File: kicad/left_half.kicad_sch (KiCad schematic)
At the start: 36 parts, among them SW1 SW_Push, SW10 SW_Push, SW11 SW_Push, SW12 SW_Push, SW13 SW_Push, SW14 SW_Push, SW15 SW_Push, SW16 SW_Push, SW17 SW_Push, SW18 SW_Push, SW2 SW_Push, SW3 SW_Push, SW4 SW_Push, SW5 SW_Push, SW6 SW_Push, SW7 SW_Push, SW8 SW_Push, SW9 SW_Push

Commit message: WiP: add schematic for the keyboard
- add full schematics for both halves
- add footprints and symbols for peripherals
- PIR still needs symbol + footprint
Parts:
- added J1: Conn_01x03_Pin, symbol Connector:Conn_01x03_Pin
- added J2: AudioJack4, symbol Connector_Audio:AudioJack4
- added R1: R_Photo, symbol Device:R_Photo
- added R2: R, symbol Device:R
- added U1: RP2040-Zero, symbol RP2040-Zero:RP2040-Zero
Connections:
- net C1: now reaches D1.1 (K), D10.1 (K), D11.1 (K), D12.1 (K), D13.1 (K), D14.1 (K), D15.1 (K), D16.1 (K), D17.1 (K), D18.1 (K), D2.1 (K), D3.1 (K), D4.1 (K), D5.1 (K), D6.1 (K), D7.1 (K), D8.1 (K), D9.1 (K), SW1.2, SW10.2, SW11.2, SW12.2, SW13.2, SW14.2, SW15.2, SW16.2, SW17.2, SW18.2, SW2.2, SW3.2, SW4.2, SW5.2, SW6.2, SW7.2, SW8.2, SW9.2
- net C1: now also U1.10, U1.11, U1.12, U1.13, U1.5, U1.6, U1.7, U1.8, U1.9
- new net ADC0: R1.2, R2.2, U1.26
- new net GND: J1.1 (Pin_1), J2.S, R2.1, U1.GND
- new net OUT: J1.2 (Pin_2), U1.28
- new net Rx: J2.R2, U1.1
- new net Tx: J2.R1, U1.0
- new net VCC: J1.3 (Pin_3), J2.T, R1.1, U1.3v3

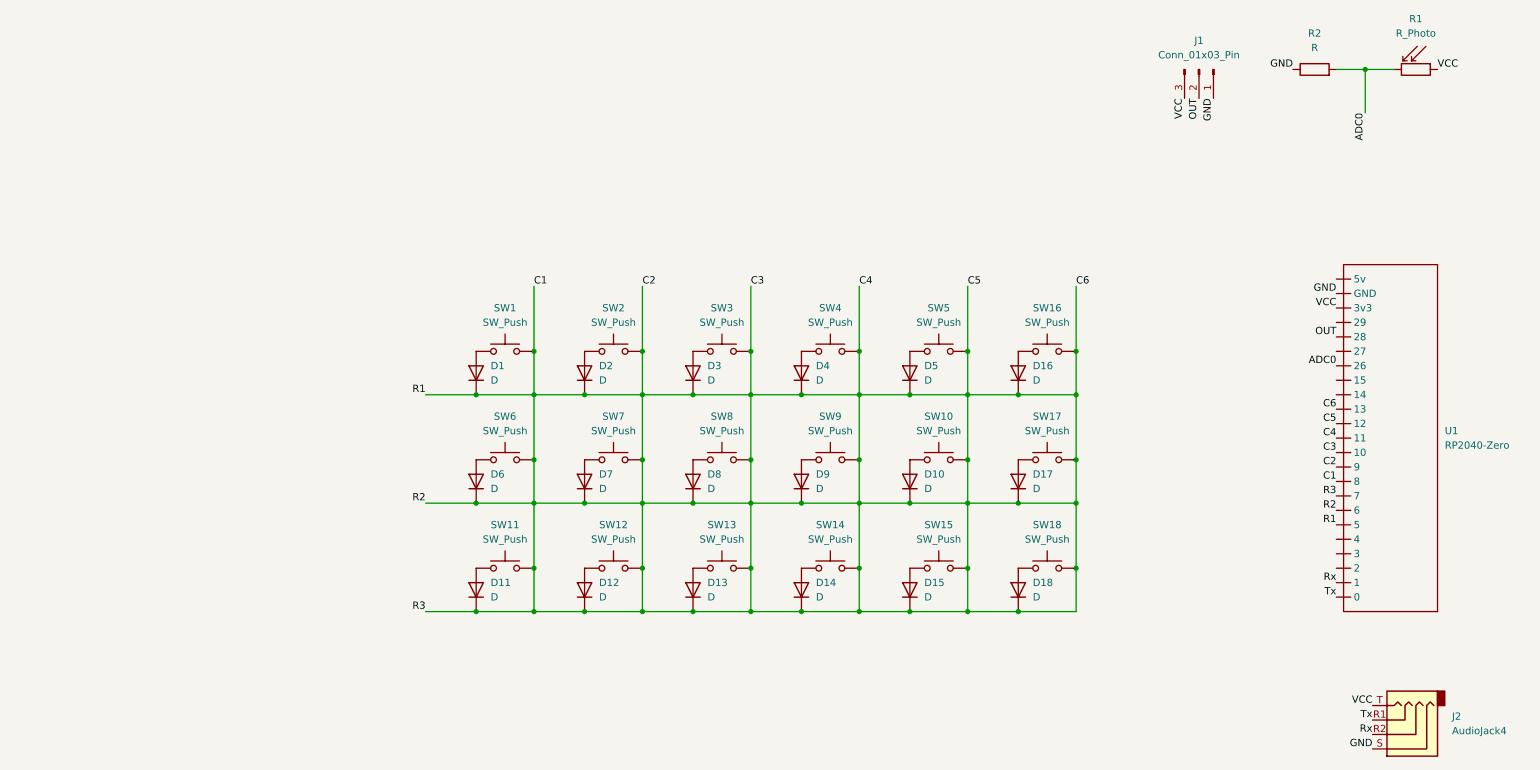
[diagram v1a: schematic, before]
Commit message: feat: add SK6812 per key lighting
- every key is illuminated by a SK6812 RGB LED
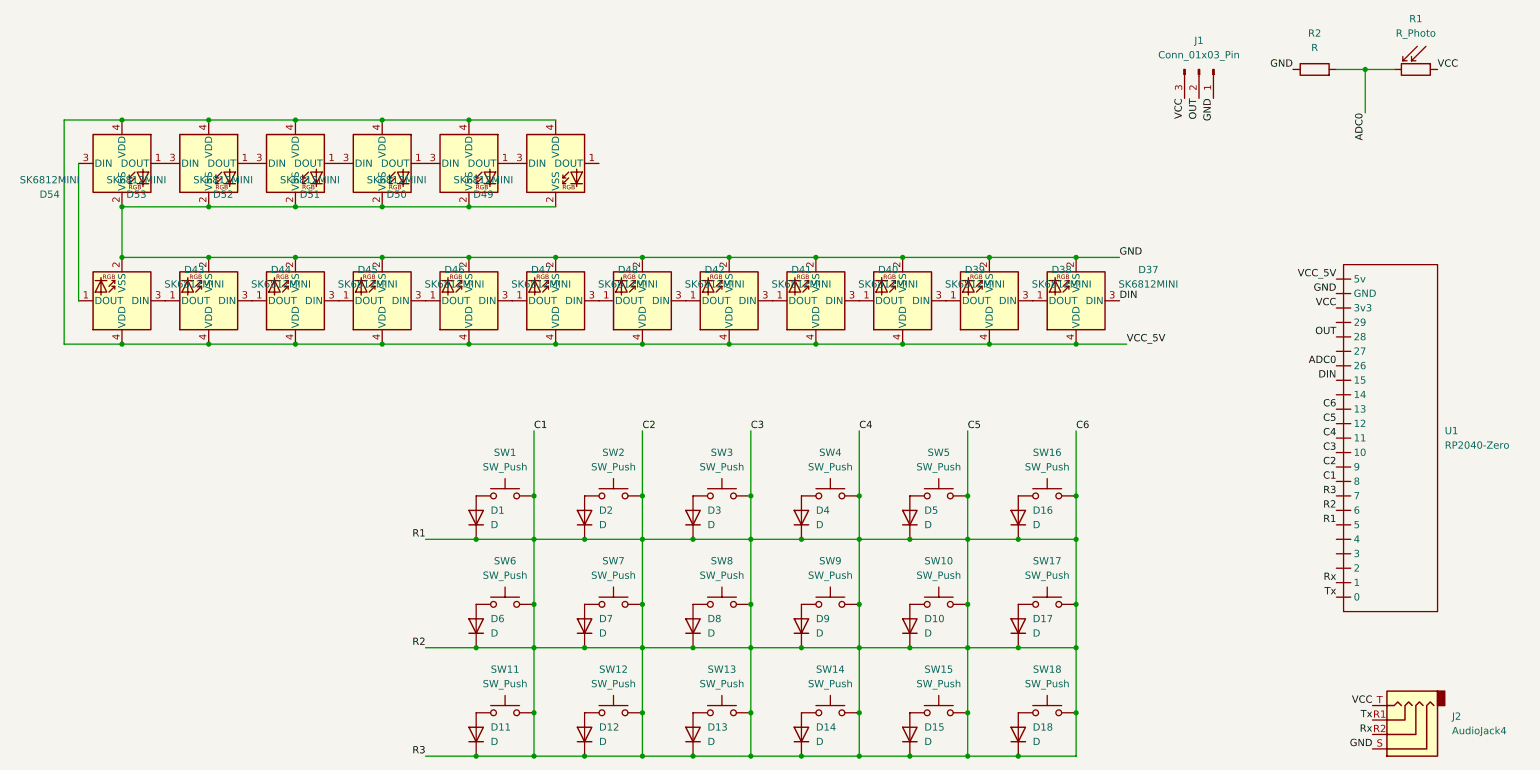
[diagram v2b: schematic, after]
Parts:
- added D37, D38, D39, D40, D41, D42, D43, D44, D45, D46, D47, D48, D49, D50, D51, D52, D53, D54: SK6812MINI, LED_SMD:LED_SK6812MINI_PLCC4_3.5x3.5mm_P1.75mm, symbol LED:SK6812MINI
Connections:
- net GND: now also D37.2 (VSS), D38.2 (VSS), D39.2 (VSS), D40.2 (VSS), D41.2 (VSS), D42.2 (VSS), D43.2 (VSS), D44.2 (VSS), D45.2 (VSS), D46.2 (VSS), D47.2 (VSS), D48.2 (VSS), D49.2 (VSS), D50.2 (VSS), D51.2 (VSS), D52.2 (VSS), D53.2 (VSS), D54.2 (VSS)
- net DIN: now reaches U1.15
- net DIN: now also D37.3 (DIN)
- net VCC_5V: now reaches U1.5v
- net VCC_5V: now also D37.4 (VDD), D38.4 (VDD), D39.4 (VDD), D40.4 (VDD), D41.4 (VDD), D42.4 (VDD), D43.4 (VDD), D44.4 (VDD), D45.4 (VDD), D46.4 (VDD), D47.4 (VDD), D48.4 (VDD), D49.4 (VDD), D50.4 (VDD), D51.4 (VDD), D52.4 (VDD), D53.4 (VDD), D54.4 (VDD)
- new net: D49.3 (DIN), D50.1 (DOUT)
- new net: D50.3 (DIN), D51.1 (DOUT)
- new net: D40.1 (DOUT), D41.3 (DIN)
- new net: D39.1 (DOUT), D40.3 (DIN)
- new net: D43.3 (DIN), D44.1 (DOUT)
- new net: D44.3 (DIN), D45.1 (DOUT)
- new net: D53.3 (DIN), D54.1 (DOUT)
- new net: D43.1 (DOUT), D54.3 (DIN)
- new net: D51.3 (DIN), D52.1 (DOUT)
- new net: D52.3 (DIN), D53.1 (DOUT)
- new net: D38.1 (DOUT), D39.3 (DIN)
- new net: D37.1 (DOUT), D38.3 (DIN)
- new net: D45.3 (DIN), D46.1 (DOUT)
- new net: D46.3 (DIN), D47.1 (DOUT)
- new net: D47.3 (DIN), D48.1 (DOUT)
- new net: D42.1 (DOUT), D48.3 (DIN)
- new net: D41.1 (DOUT), D42.3 (DIN)
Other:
- moved on the sheet: D1, D10, D11, D12, D13, D14, D15, D16, D17, D18, D2, D3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

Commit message: apply footprints for all components
- treat column 6 as individual thumbpad file that is connected via pogo
  pins
- use generic headers for components on external boards (like OLED)
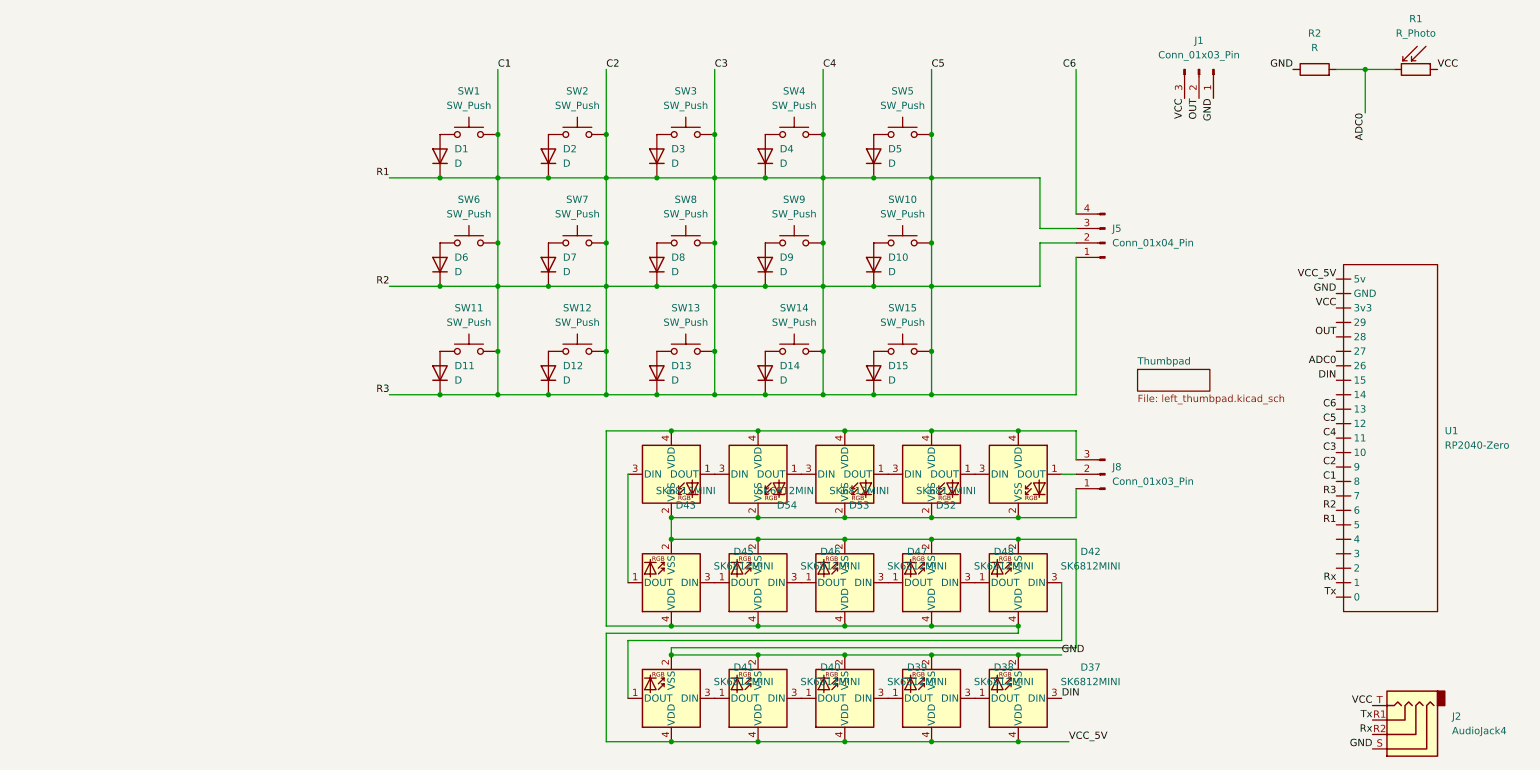
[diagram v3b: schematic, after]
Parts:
- removed D16, D17, D18: D, symbol Device:D
- removed D49, D50, D51: SK6812MINI, LED_SMD:LED_SK6812MINI_PLCC4_3.5x3.5mm_P1.75mm, symbol LED:SK6812MINI
- removed SW16, SW17, SW18: SW_Push, symbol Switch:SW_Push
- added J5: Conn_01x04_Pin, Connector_PinSocket_2.54mm:PinSocket_1x04_P2.54mm_Vertical, symbol Connector:Conn_01x04_Pin
- added J8: Conn_01x03_Pin, Connector_PinSocket_2.54mm:PinSocket_1x03_P2.54mm_Vertical, symbol Connector:Conn_01x03_Pin
- D1, D10, D11, D12, D13, D14, D15, D2, D3, D4, D5, D6, D7, D8, D9: footprint (none) -> Diode_THT:D_DO-35_SOD27_P7.62mm_Horizontal
- J1: footprint (none) -> Connector_PinHeader_2.54mm:PinHeader_1x03_P2.54mm_Vertical
- J2: footprint (none) -> PJ-320A:PJ-320A
- R1: footprint (none) -> OptoDevice:R_LDR_5.1x4.3mm_P3.4mm_Vertical
- R2: footprint (none) -> Resistor_THT:R_Axial_DIN0204_L3.6mm_D1.6mm_P7.62mm_Horizontal
- SW1, SW10, SW11, SW12, SW13, SW14, SW15, SW2, SW3, SW4, SW5, SW6, SW7, SW8, SW9: footprint (none) -> Choc-V1:Kailh-PG1353-Solderable-1U
- U1: footprint (none) -> RP2040-Zero:RP2040-Zero
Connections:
- net C1: now also J5.1 (Pin_1), J5.2 (Pin_2), J5.3 (Pin_3); no longer U1.13
- net GND: now also J8.1 (Pin_1)
- net VCC_5V: now also J8.3 (Pin_3)
- net at D52.1 (DOUT): now also J8.2 (Pin_2)
- new net C6: J5.4 (Pin_4), U1.13
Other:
- added sheet Thumbpad (left_thumbpad.kicad_sch)
- moved on the sheet: D1, D10, D11, D12, D13, D14, D15, D2, D3, D37, D38, D39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

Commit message: wip: add PCB
- started working on the actual PCB
- however this will be subject to change later
- add footprint for sk6812-mini-e LEDs
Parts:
- D37, D38, D39, D40, D41, D42, D43, D44, D45, D46, D47, D48, D52, D53, D54: footprint LED_SMD:LED_SK6812MINI_PLCC4_3.5x3.5mm_P1.75mm -> SK6812-Mini-E:MX_SK6812MINI-E
- SW1, SW10, SW11, SW12, SW13, SW14, SW15, SW2, SW3, SW4, SW5, SW6, SW7, SW8, SW9: footprint Choc-V1:Kailh-PG1353-Solderable-1U -> Choc-V1:SW_Kailh_Choc_V1
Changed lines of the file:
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@@
 			)
 		)
-		(property "Footprint" "LED_SMD:LED_SK6812MINI_PLCC4_3.5x3.5mm_P1.75mm"
+		(property "Footprint" "SK6812-Mini-E:MX_SK6812MINI-E"
 			(at 133.35 134.62 0)
 			(effects
@@
 			)
 		)
-		(property "Footprint" "Choc-V1:Kailh-PG1353-Solderable-1U"
+		(property "Footprint" "Choc-V1:SW_Kailh_Choc_V1"
 			(at 83.82 57.15 0)
 			(effects
@@
 			)
 		)
-		(property "Footprint" "Choc-V1:Kailh-PG1353-Solderable-1U"
+		(property "Footprint" "Choc-V1:SW_Kailh_Choc_V1"
 			(at 140.97 76.2 0)
 			(effects
@@
 			)
 		)
-		(property "Footprint" "Choc-V1:Kailh-PG1353-Solderable-1U"
+		(property "Footprint" "Choc-V1:SW_Kailh_Choc_V1"
 			(at 160.02 57.15 0)
 			(effects
@@
 			)
 		)
-		(property "Footprint" "LED_SMD:LED_SK6812MINI_PLCC4_3.5x3.5mm_P1.75mm"
+		(property "Footprint" "SK6812-Mini-E:MX_SK6812MINI-E"
 			(at 120.65 110.49 0)
 			(effects
@@
 			)
 		)
-		(property "Footprint" "Choc-V1:Kailh-PG1353-Solderable-1U"
+		(property "Footprint" "Choc-V1:SW_Kailh_Choc_V1"
 			(at 121.92 76.2 0)
 			(effects
@@
 			)
 		)
-		(property "Footprint" "LED_SMD:LED_SK6812MINI_PLCC4_3.5x3.5mm_P1.75mm"
+		(property "Footprint" "SK6812-Mini-E:MX_SK6812MINI-E"
 			(at 151.13 110.49 0)
 			(effects
@@
 			)
 		)
-		(property "Footprint" "Choc-V1:Kailh-PG1353-Solderable-1U"
+		(property "Footprint" "Choc-V1:SW_Kailh_Choc_V1"
 			(at 140.97 38.1 0)
 			(effects
@@
 			)
 		)
-		(property "Footprint" "Choc-V1:Kailh-PG1353-Solderable-1U"
+		(property "Footprint" "Choc-V1:SW_Kailh_Choc_V1"
 			(at 83.82 38.1 0)
 			(effects
@@
 			)
 		)
-		(property "Footprint" "LED_SMD:LED_SK6812MINI_PLCC4_3.5x3.5mm_P1.75mm"
+		(property "Footprint" "SK6812-Mini-E:MX_SK6812MINI-E"
 			(at 181.61 110.49 0)
 			(effects
@@
 			)
 		)
-		(property "Footprint" "LED_SMD:LED_SK6812MINI_PLCC4_3.5x3.5mm_P1.75mm"
+		(property "Footprint" "SK6812-Mini-E:MX_SK6812MINI-E"
 			(at 148.59 134.62 0)
 			(effects
@@
 			)
 		)
-		(property "Footprint" "LED_SMD:LED_SK6812MINI_PLCC4_3.5x3.5mm_P1.75mm"
+		(property "Footprint" "SK6812-Mini-E:MX_SK6812MINI-E"
 			(at 135.89 110.49 0)
 			(effects
@@
 			)
 		)
-		(property "Footprint" "Choc-V1:Kailh-PG1353-Solderable-1U"
+		(property "Footprint" "Choc-V1:SW_Kailh_Choc_V1"
 			(at 160.02 38.1 0)
 			(effects
@@
 			)
 		)
-		(property "Footprint" "Choc-V1:Kailh-PG1353-Solderable-1U"
+		(property "Footprint" "Choc-V1:SW_Kailh_Choc_V1"
 			(at 121.92 38.1 0)
 			(effects
@@
 			)
 		)
-		(property "Footprint" "LED_SMD:LED_SK6812MINI_PLCC4_3.5x3.5mm_P1.75mm"
+		(property "Footprint" "SK6812-Mini-E:MX_SK6812MINI-E"
 			(at 179.07 134.62 0)
 			(effects
@@
 			)
 		)
-		(property "Footprint" "LED_SMD:LED_SK6812MINI_PLCC4_3.5x3.5mm_P1.75mm"
+		(property "Footprint" "SK6812-Mini-E:MX_SK6812MINI-E"
 			(at 118.11 114.3 0)
 			(effects
@@
 			)
 		)
-		(property "Footprint" "LED_SMD:LED_SK6812MINI_PLCC4_3.5x3.5mm_P1.75mm"
+		(property "Footprint" "SK6812-Mini-E:MX_SK6812MINI-E"
 			(at 133.35 114.3 0)
 			(effects
@@
 			)
 		)
-		(property "Footprint" "LED_SMD:LED_SK6812MINI_PLCC4_3.5x3.5mm_P1.75mm"
+		(property "Footprint" "SK6812-Mini-E:MX_SK6812MINI-E"
 			(at 163.83 134.62 0)
 			(effects
@@
 			)
 		)
-		(property "Footprint" "LED_SMD:LED_SK6812MINI_PLCC4_3.5x3.5mm_P1.75mm"
+		(property "Footprint" "SK6812-Mini-E:MX_SK6812MINI-E"
 			(at 163.83 114.3 0)
 			(effects
@@
 			)
 		)
-		(property "Footprint" "LED_SMD:LED_SK6812MINI_PLCC4_3.5x3.5mm_P1.75mm"
+		(property "Footprint" "SK6812-Mini-E:MX_SK6812MINI-E"
 			(at 118.11 134.62 0)
 			(effects
@@
 			)
 		)
-		(property "Footprint" "LED_SMD:LED_SK6812MINI_PLCC4_3.5x3.5mm_P1.75mm"
+		(property "Footprint" "SK6812-Mini-E:MX_SK6812MINI-E"
 			(at 166.37 110.49 0)
 			(effects
@@
 			)
 		)
-		(property "Footprint" "Choc-V1:Kailh-PG1353-Solderable-1U"
+		(property "Footprint" "Choc-V1:SW_Kailh_Choc_V1"
 			(at 102.87 76.2 0)
 			(effects
@@
 			)
 		)
-		(property "Footprint" "Choc-V1:Kailh-PG1353-Solderable-1U"
+		(property "Footprint" "Choc-V1:SW_Kailh_Choc_V1"
 			(at 121.92 57.15 0)
 			(effects
@@
 			)
 		)
-		(property "Footprint" "Choc-V1:Kailh-PG1353-Solderable-1U"
+		(property "Footprint" "Choc-V1:SW_Kailh_Choc_V1"
 			(at 102.87 38.1 0)
 			(effects
@@
 			)
 		)
-		(property "Footprint" "Choc-V1:Kailh-PG1353-Solderable-1U"
+		(property "Footprint" "Choc-V1:SW_Kailh_Choc_V1"
 			(at 102.87 57.15 0)
 			(effects
@@
 			)
 		)
-		(property "Footprint" "Choc-V1:Kailh-PG1353-Solderable-1U"
+		(property "Footprint" "Choc-V1:SW_Kailh_Choc_V1"
 			(at 160.02 76.2 0)
 			(effects
@@
 			)
 		)
-		(property "Footprint" "Choc-V1:Kailh-PG1353-Solderable-1U"
+		(property "Footprint" "Choc-V1:SW_Kailh_Choc_V1"
 			(at 140.97 57.15 0)
 			(effects
@@
 			)
 		)
-		(property "Footprint" "Choc-V1:Kailh-PG1353-Solderable-1U"
+		(property "Footprint" "Choc-V1:SW_Kailh_Choc_V1"
 			(at 83.82 76.2 0)
 			(effects
@@
 			)
 		)
-		(property "Footprint" "LED_SMD:LED_SK6812MINI_PLCC4_3.5x3.5mm_P1.75mm"
+		(property "Footprint" "SK6812-Mini-E:MX_SK6812MINI-E"
 			(at 148.59 114.3 0)
 			(effects
@@
 			)
 		)
-		(property "Footprint" "LED_SMD:LED_SK6812MINI_PLCC4_3.5x3.5mm_P1.75mm"
+		(property "Footprint" "SK6812-Mini-E:MX_SK6812MINI-E"
 			(at 179.07 114.3 0)
 			(effects

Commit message: wip: pcb for both halves
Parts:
- removed J2: AudioJack4, PJ-320A:PJ-320A, symbol Connector_Audio:AudioJack4
- added J2: AudioJack4, PJ-320A:PJ-320A, symbol PJ-320A:AudioJack4
- SW1, SW10, SW11, SW12, SW13, SW14, SW15, SW2, SW3, SW4, SW5, SW6, SW7, SW8, SW9: footprint Choc-V1:SW_Kailh_Choc_V1 -> Choc-V1:SW_Kailh_Choc_V1_THT
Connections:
- net C1: no longer D1.1 (K), D10.1 (K), D11.1 (K), D12.1 (K), D13.1 (K), D14.1 (K), D15.1 (K), D2.1 (K), D3.1 (K), D4.1 (K), D5.1 (K), D6.1 (K), D7.1 (K), D8.1 (K), D9.1 (K), J5.1 (Pin_1), J5.2 (Pin_2), J5.3 (Pin_3), SW10.2, SW12.2, SW13.2, SW14.2, SW15.2, SW2.2, SW3.2, SW4.2, SW5.2, SW7.2, SW8.2, SW9.2, U1.10, U1.11, U1.12, U1.5, U1.6, U1.7, U1.8
- net C6: now also U1.5; no longer U1.13
- net GND: now also J2.1
- net OUT: now also R1.1; no longer U1.28
- net Rx: now also J2.4
- net Tx: now also J2.3
- removed net VCC: J1.3 (Pin_3), R1.1, U1.3v3
- net VCC_5V renamed +5V
- net +5V: now also J1.3 (Pin_3), J2.2
- new net C2: SW12.2, SW2.2, SW7.2, U1.10
- new net C3: SW13.2, SW3.2, SW8.2, U1.11
- new net C4: SW14.2, SW4.2, SW9.2, U1.12
- new net C5: SW10.2, SW15.2, SW5.2, U1.13
- new net R1: D1.1 (K), D2.1 (K), D3.1 (K), D4.1 (K), D5.1 (K), J5.3 (Pin_3), U1.6
- new net R2: D10.1 (K), D6.1 (K), D7.1 (K), D8.1 (K), D9.1 (K), J5.2 (Pin_2), U1.7
- new net R3: D11.1 (K), D12.1 (K), D13.1 (K), D14.1 (K), D15.1 (K), J5.1 (Pin_1), U1.8
